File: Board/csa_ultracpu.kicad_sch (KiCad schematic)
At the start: 0 parts

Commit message: work on hdmi
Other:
- note added: "CSA-ULTRACPU-V2.2A"
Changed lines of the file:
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@@
 	(generator_version "9.0")
 	(paper "A4")
-	(sheet
-		(at 228.6 25.4)
+	(text "CSA-ULTRACPU-V2.2A"
+		(exclude_from_sim no)
+		(at 194.31 172.72 0)
+		(effects
+			(font
+				(size 3.81 3.2385)
+			)
+			(justify left bottom)
+		)
+	)
+	(bus
+		(pts
+			(xy 287.02 38.735) (xy 33.655 38.735)
+		)
+		(stroke
+			(width 0)
+			(type default)
+		)
+	)
+	(bus
+		(pts
+			(xy 33.655 38.735) (xy 33.655 199.39)
+		)
+		(stroke
+			(width 0)
+			(type default)
+		)
+	)
+	(bus
+		(pts
+			(xy 287.02 199.39) (xy 287.02 38.735)
+		)
+		(stroke
+			(width 0)
+			(type default)
+		)
+	)
+	(bus
+		(pts
+			(xy 33.655 199.39) (xy 287.02 199.39)
+		)
+		(stroke
+			(width 0)
+			(type default)
+		)
+	)
+	(symbol
+		(lib_id "csa_ultracpu-eagle-import:DOCFIELD")
+		(at 185.42 199.39 0)
+		(unit 1)
+		(exclude_from_sim no)
+		(in_bom yes)
+		(on_board yes)
+		(dnp no)
+		(property "Reference" "#FRAME7"
+			(at 185.42 199.39 0)
+			(effects
+				(font
+					(size 1.27 1.27)
+				)
+				(hide yes)
+			)
+		)
+		(property "Value" "DOCFIELD"
+			(at 185.42 199.39 0)
+			(effects
+				(font
+					(size 1.27 1.27)
+				)
+				(hide yes)
+			)
+		)
+		(property "Footprint" ""
+			(at 185.42 199.39 0)
+			(effects
+				(font
+					(size 1.27 1.27)
+				)
+				(hide yes)
+			)
+		)
+		(property "Datasheet" ""
+			(at 185.42 199.39 0)
+			(effects
+				(font
+					(size 1.27 1.27)
+				)
+				(hide yes)
+			)
+		)
+		(property "Description" ""
+			(at 185.42 199.39 0)
+			(effects
+				(font
+					(size 1.27 1.27)
+				)
+				(hide yes)
+			)
+		)
+		(instances
+			(project "csa_ultracpu"
+				(path "/381336a5-a662-4c84-a650-90475fa59a97"
+					(reference "#FRAME7")
+					(unit 1)
+				)
+			)
+		)
+	)
+	(sheet
+		(at 189.23 102.87)
 		(size 12.7 3.81)
 		(exclude_from_sim no)
@@
 		)
 		(property "Sheetname" "USB"
-			(at 228.6 24.6884 0)
+			(at 189.23 102.1584 0)
 			(effects
 				(font
@@
 		)
 		(property "Sheetfile" "USB.kicad_sch"
-			(at 228.6 29.7946 0)
+			(at 189.23 107.2646 0)
 			(effects
 				(font
@@
 	)
 	(sheet
-		(at 177.8 25.4)
+		(at 138.43 102.87)
 		(size 12.7 3.81)
 		(exclude_from_sim no)
@@
 		)
 		(property "Sheetname" "A/V Out"
-			(at 177.8 24.6884 0)
+			(at 138.43 102.1584 0)
 			(effects
 				(font
@@
 		)
 		(property "Sheetfile" "A%2fV_Out.kicad_sch"
-			(at 177.8 29.7946 0)
+			(at 138.43 107.2646 0)
 			(effects
 				(font
@@
 	)
 	(sheet
-		(at 25.4 25.4)
+		(at 85.09 77.47)
 		(size 12.7 3.81)
 		(exclude_from_sim no)
@@
 		)
 		(property "Sheetname" "BUS I/O"
-			(at 25.4 24.6884 0)
+			(at 85.09 76.7584 0)
 			(effects
 				(font
@@
 		)
 		(property "Sheetfile" "BUS_I%2fO.kicad_sch"
-			(at 25.4 29.7946 0)
+			(at 85.09 81.8646 0)
 			(effects
 				(font
@@
 	)
 	(sheet
-		(at 25.4 76.2)
+		(at 85.09 101.6)
 		(size 12.7 3.81)
 		(exclude_from_sim no)
@@
 		)
 		(property "Sheetname" "Audio/Video"
-			(at 25.4 75.4884 0)
+			(at 85.09 100.8884 0)
 			(effects
 				(font
@@
 		)
 		(property "Sheetfile" "Audio%2fVideo.kicad_sch"
-			(at 25.4 80.5946 0)
+			(at 85.09 105.9946 0)
 			(effects
 				(font
@@
 	)
 	(sheet
-		(at 127 25.4)
+		(at 186.69 77.47)
 		(size 12.7 3.81)
 		(exclude_from_sim no)
@@
 		)
 		(property "Sheetname" "Power"
-			(at 127 24.6884 0)
+			(at 186.69 76.7584 0)
 			(effects
 				(font
@@
 		)
 		(property "Sheetfile" "Power.kicad_sch"
-			(at 127 29.7946 0)
+			(at 186.69 81.8646 0)
 			(effects
 				(font
@@
 	)
 	(sheet
-		(at 76.2 25.4)
+		(at 135.89 77.47)
 		(size 12.7 3.81)
 		(exclude_from_sim no)
@@
 		)
 		(property "Sheetname" "CPU,RAM,ROM"
-			(at 76.2 24.6884 0)
+			(at 135.89 76.7584 0)
 			(effects
 				(font
@@
 		)
 		(property "Sheetfile" "CPU,RAM,ROM.kicad_sch"
-			(at 76.2 29.7946 0)
-			(effects
-				(font
+			(at 135.89 81.8646 0)
+			(effects
+				(font

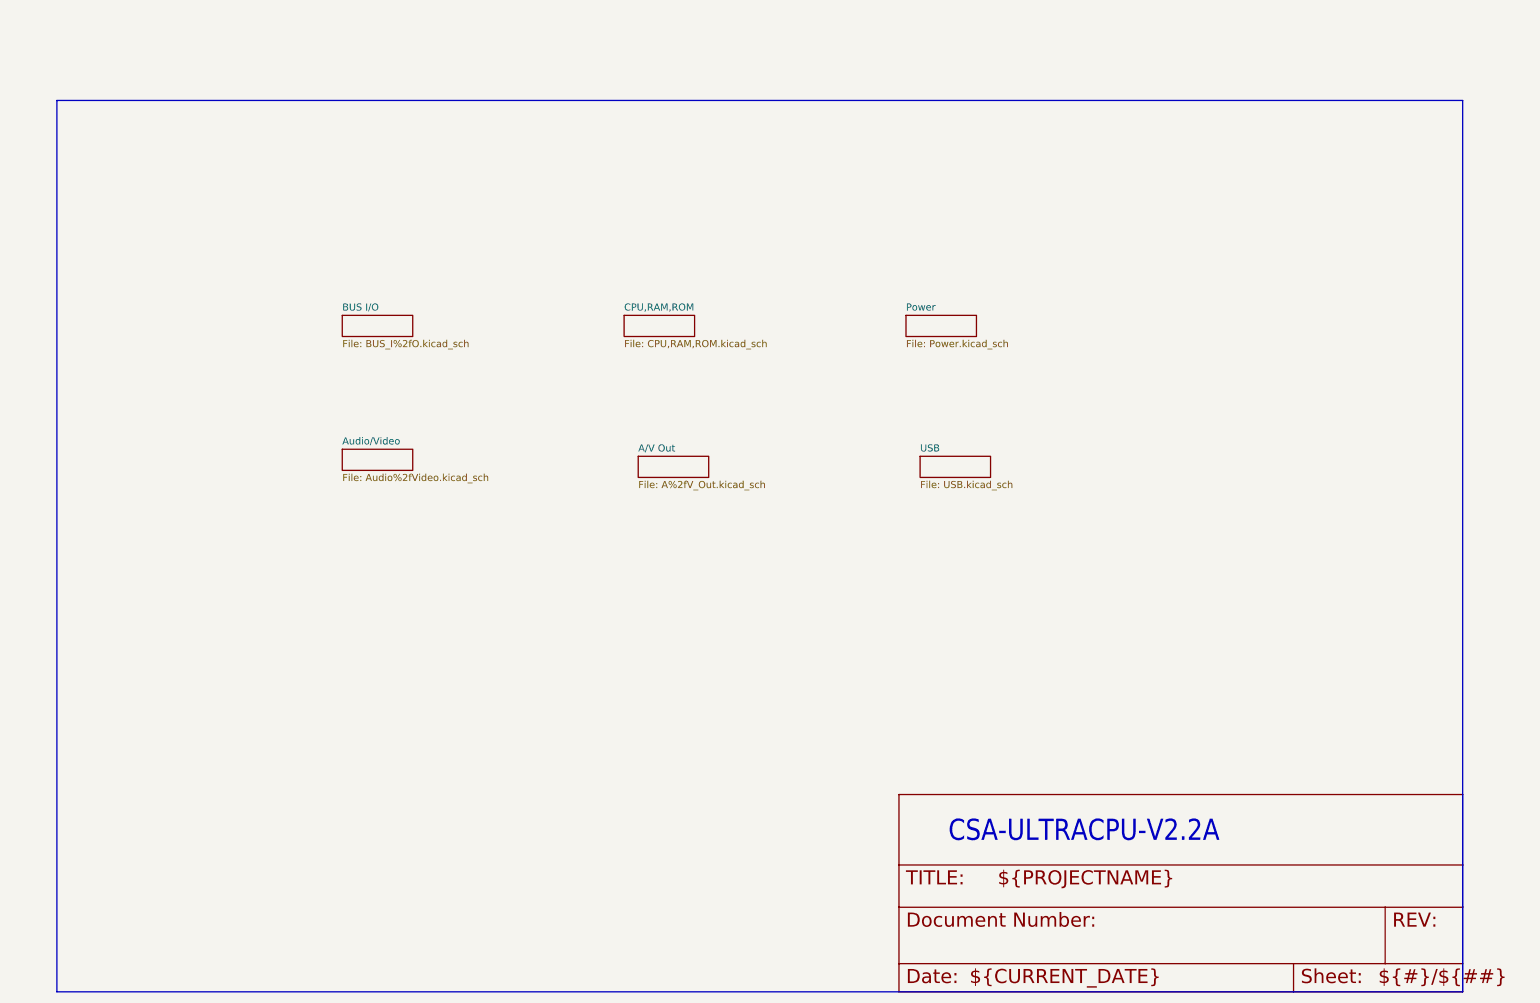
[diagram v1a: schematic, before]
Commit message: start working on 3.0 with larger FPGA
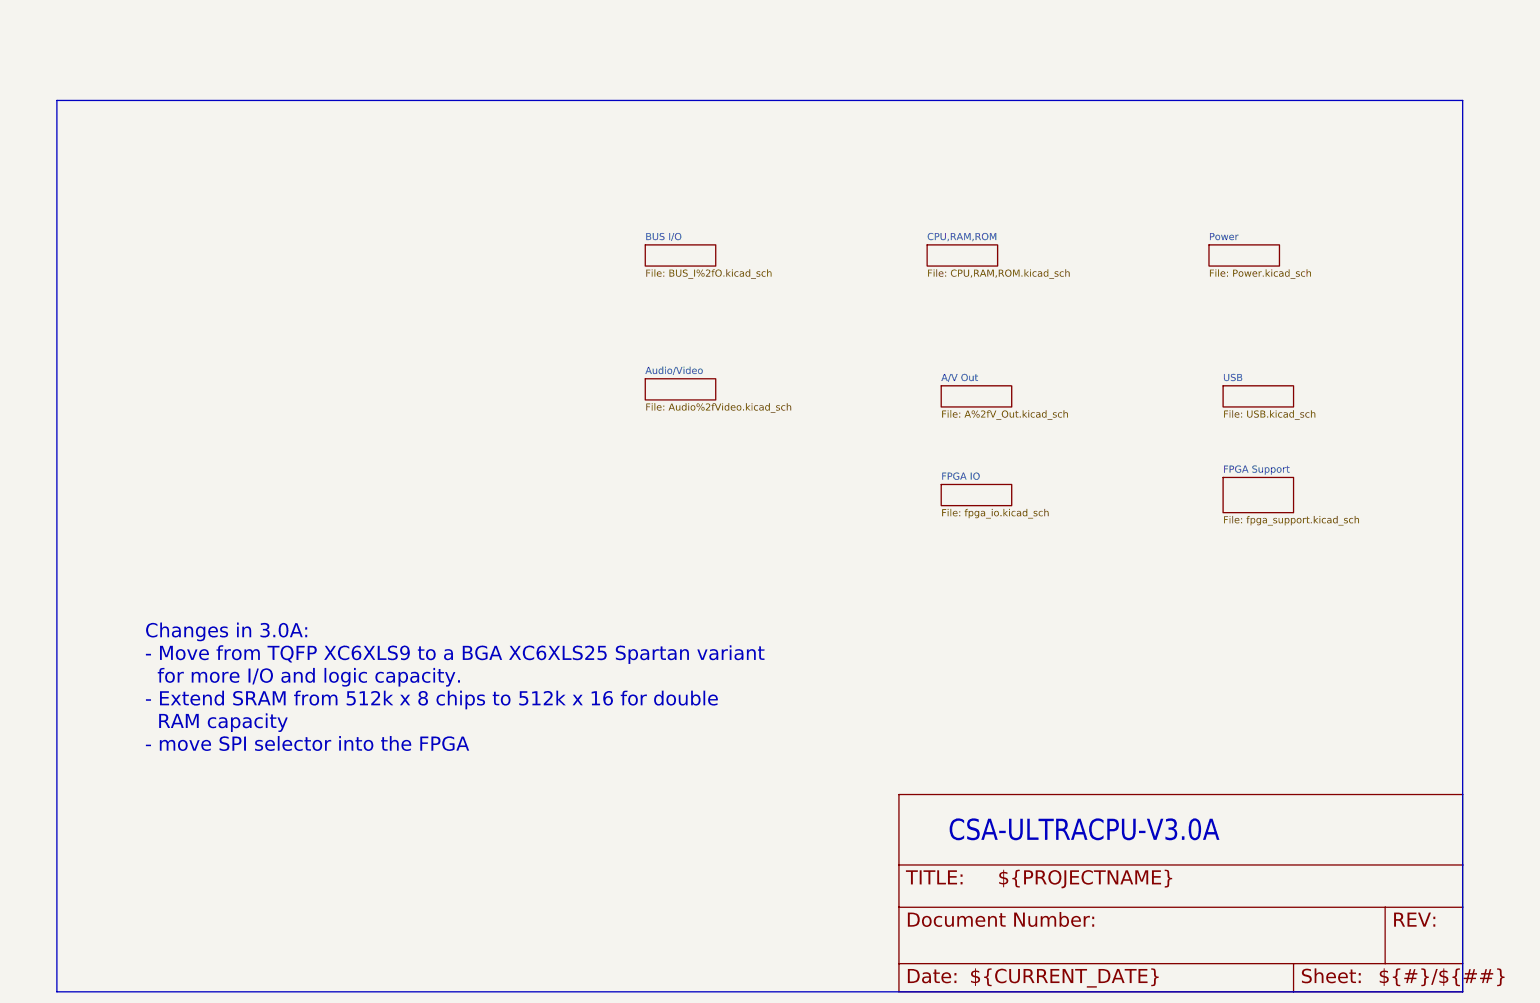
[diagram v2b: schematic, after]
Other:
- added sheet FPGA IO (fpga_io.kicad_sch)
- added sheet FPGA Support (fpga_support.kicad_sch)
- note added: "CSA-ULTRACPU-V3.0A"
- note added: "Changes in 3.0A: - Move from TQFP XC6XLS9 to a BGA XC6XLS25 Spartan variant for more I/O and logic capacity. - Extend SRAM from 512k x 8 chips to 512k x 16 for double RAM capacity - move SPI selector into the FPGA"
- note removed: "CSA-ULTRACPU-V2.2A"
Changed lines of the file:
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@@
 	(generator_version "9.0")
 	(paper "A4")
-	(text "CSA-ULTRACPU-V2.2A"
+	(text "Changes in 3.0A:\n- Move from TQFP XC6XLS9 to a BGA XC6XLS25 Spartan variant \n  for more I/O and logic capacity.\n- Extend SRAM from 512k x 8 chips to 512k x 16 for double \n  RAM capacity\n- move SPI selector into the FPGA\n"
+		(exclude_from_sim no)
+		(at 49.53 144.78 0)
+		(effects
+			(font
+				(size 2.54 2.54)
+			)
+			(justify left)
+		)
+	)
+	(text "CSA-ULTRACPU-V3.0A"
 		(exclude_from_sim no)
 		(at 194.31 172.72 0)
@@
 	)
 	(sheet
-		(at 189.23 102.87)
+		(at 243.84 90.17)
 		(size 12.7 3.81)
 		(exclude_from_sim no)
@@
 		)
 		(property "Sheetname" "USB"
-			(at 189.23 102.1584 0)
+			(at 243.84 89.4584 0)
 			(effects
 				(font
@@
 		)
 		(property "Sheetfile" "USB.kicad_sch"
-			(at 189.23 107.2646 0)
+			(at 243.84 94.5646 0)
 			(effects
 				(font
@@
 	)
 	(sheet
-		(at 138.43 102.87)
+		(at 193.04 90.17)
 		(size 12.7 3.81)
 		(exclude_from_sim no)
@@
 		)
 		(property "Sheetname" "A/V Out"
-			(at 138.43 102.1584 0)
+			(at 193.04 89.4584 0)
 			(effects
 				(font
@@
 		)
 		(property "Sheetfile" "A%2fV_Out.kicad_sch"
-			(at 138.43 107.2646 0)
+			(at 193.04 94.5646 0)
 			(effects
 				(font
@@
 	)
 	(sheet
-		(at 85.09 77.47)
+		(at 139.7 64.77)
 		(size 12.7 3.81)
 		(exclude_from_sim no)
@@
 		)
 		(property "Sheetname" "BUS I/O"
-			(at 85.09 76.7584 0)
+			(at 139.7 64.0584 0)
 			(effects
 				(font
@@
 		)
 		(property "Sheetfile" "BUS_I%2fO.kicad_sch"
-			(at 85.09 81.8646 0)
+			(at 139.7 69.1646 0)
 			(effects
 				(font
@@
 	)
 	(sheet
-		(at 85.09 101.6)
+		(at 243.84 106.68)
+		(size 12.7 6.35)
+		(exclude_from_sim no)
+		(in_bom yes)
+		(on_board yes)
+		(dnp no)
+		(fields_autoplaced yes)
+		(stroke
+			(width 0.1524)
+			(type solid)
+		)
+		(fill
+			(color 0 0 0 0.0000)
+		)
+		(property "Sheetname" "FPGA Support"
+			(at 243.84 105.9684 0)
+			(effects
+				(font
+					(size 1.27 1.27)
+				)
+				(justify left bottom)
+			)
+		)
+		(property "Sheetfile" "fpga_support.kicad_sch"
+			(at 243.84 113.6146 0)
+			(effects
+				(font
+					(size 1.27 1.27)
+				)
+				(justify left top)
+			)
+		)
+		(instances
+			(project "csa_ultracpu"
+				(path "/381336a5-a662-4c84-a650-90475fa59a97"
+					(page "8")
+				)
+			)
+		)
+	)
+	(sheet
+		(at 139.7 88.9)
 		(size 12.7 3.81)
 		(exclude_from_sim no)
@@
 		)
 		(property "Sheetname" "Audio/Video"
-			(at 85.09 100.8884 0)
+			(at 139.7 88.1884 0)
 			(effects
 				(font
@@
 		)
 		(property "Sheetfile" "Audio%2fVideo.kicad_sch"
-			(at 85.09 105.9946 0)
+			(at 139.7 93.2946 0)
 			(effects
 				(font
@@
 	)
 	(sheet
-		(at 186.69 77.47)
+		(at 241.3 64.77)
 		(size 12.7 3.81)
 		(exclude_from_sim no)
@@
 		)
 		(property "Sheetname" "Power"
-			(at 186.69 76.7584 0)
+			(at 241.3 64.0584 0)
 			(effects
 				(font
@@
 		)
 		(property "Sheetfile" "Power.kicad_sch"
-			(at 186.69 81.8646 0)
+			(at 241.3 69.1646 0)
 			(effects
 				(font
@@
 	)
 	(sheet
-		(at 135.89 77.47)
+		(at 193.04 107.95)
+		(size 12.7 3.81)
+		(exclude_from_sim no)
+		(in_bom yes)
+		(on_board yes)
+		(dnp no)
+		(fields_autoplaced yes)
+		(stroke
+			(width 0.1524)
+			(type solid)
+		)
+		(fill
+			(color 0 0 0 0.0000)
+		)
+		(property "Sheetname" "FPGA IO"
+			(at 193.04 107.2384 0)
+			(effects
+				(font
+					(size 1.27 1.27)
+				)
+				(justify left bottom)
+			)
+		)
+		(property "Sheetfile" "fpga_io.kicad_sch"
+			(at 193.04 112.3446 0)
+			(effects
+				(font
+					(size 1.27 1.27)
+				)
+				(justify left top)
+			)
+		)
+		(instances
+			(project "csa_ultracpu"
+				(path "/381336a5-a662-4c84-a650-90475fa59a97"
+					(page "9")
+				)
+			)
+		)
+	)
+	(sheet
+		(at 190.5 64.77)
 		(size 12.7 3.81)
 		(exclude_from_sim no)
@@
 		)
 		(property "Sheetname" "CPU,RAM,ROM"
-			(at 135.89 76.7584 0)
+			(at 190.5 64.0584 0)
 			(effects
 				(font
@@
 		)
 		(property "Sheetfile" "CPU,RAM,ROM.kicad_sch"
-			(at 135.89 81.8646 0)
-			(effects
-				(font
+			(at 190.5 69.1646 0)
+			(effects
+				(font
